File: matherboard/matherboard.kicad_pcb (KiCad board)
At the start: 2 copper layers, 17 parts, among them J1 RJ12, J2 RJ12, J3 RJ12, P1 VCC/GND, P2 CONN_01X02, P3 CONN_01X02, P4 CONN_01X02, P5 CONN_01X05, P6 CONN_01X02, U3 STAB3.3, U4 ESP8266

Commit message: Components for BUG
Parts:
- removed P1: VCC/GND, Pin_Headers:Pin_Header_Straight_1x02
- added CON1: BARREL_JACK, Connect:BARREL_JACK, F.Cu at (134.6, 121.9)
- added U1: button, bugs:button, F.Cu at (132.1, 81.9)
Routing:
- net Net-(CON1-Pad2): track 185.8 -> 269.5 mm
- net Net-(CON1-Pad1): track 0.00 -> 51.5 mm
- net (no net): track 39.9 -> 65.8 mm
- net Net-(J1-Pad1): track 173.4 -> 168.9 mm
- net Net-(J1-Pad5): track 120.5 -> 122.7 mm
- net Net-(P2-Pad2): track 5.08 -> 4.45 mm

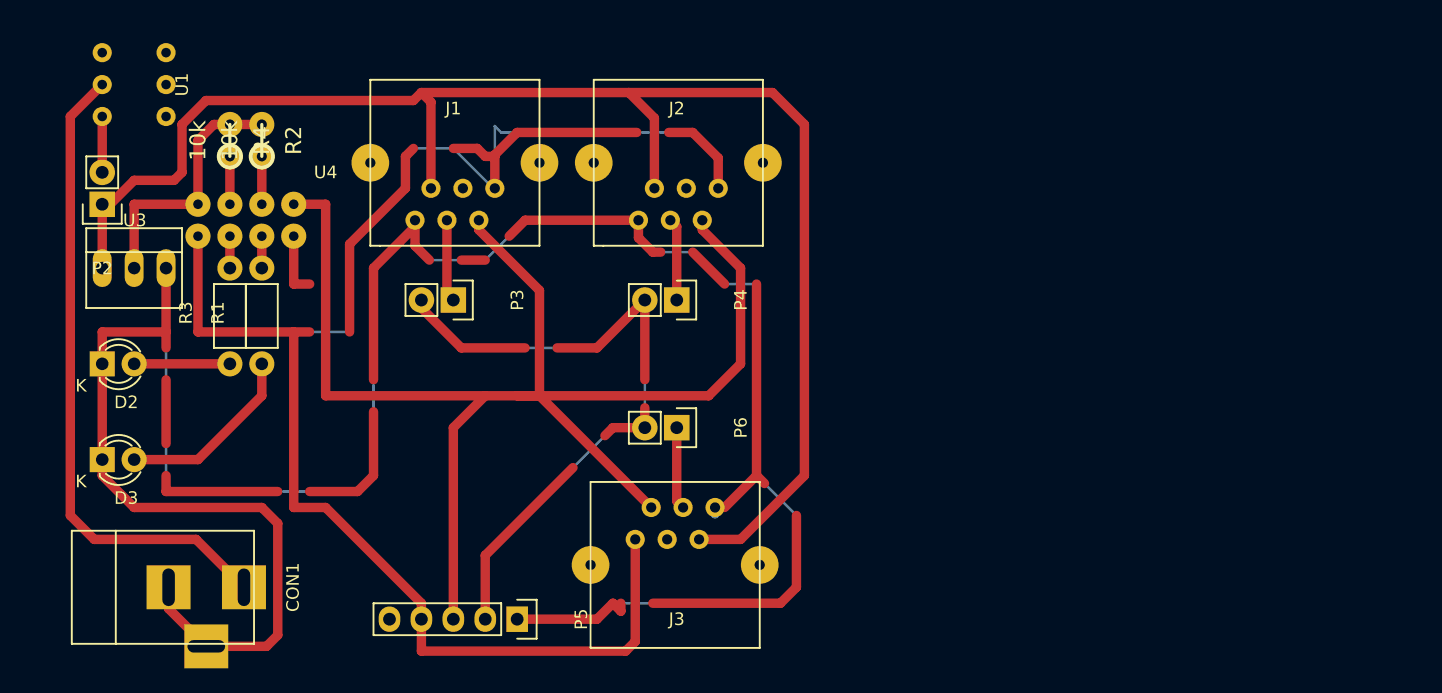
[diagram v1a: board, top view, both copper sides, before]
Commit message: Added power led to marherboard
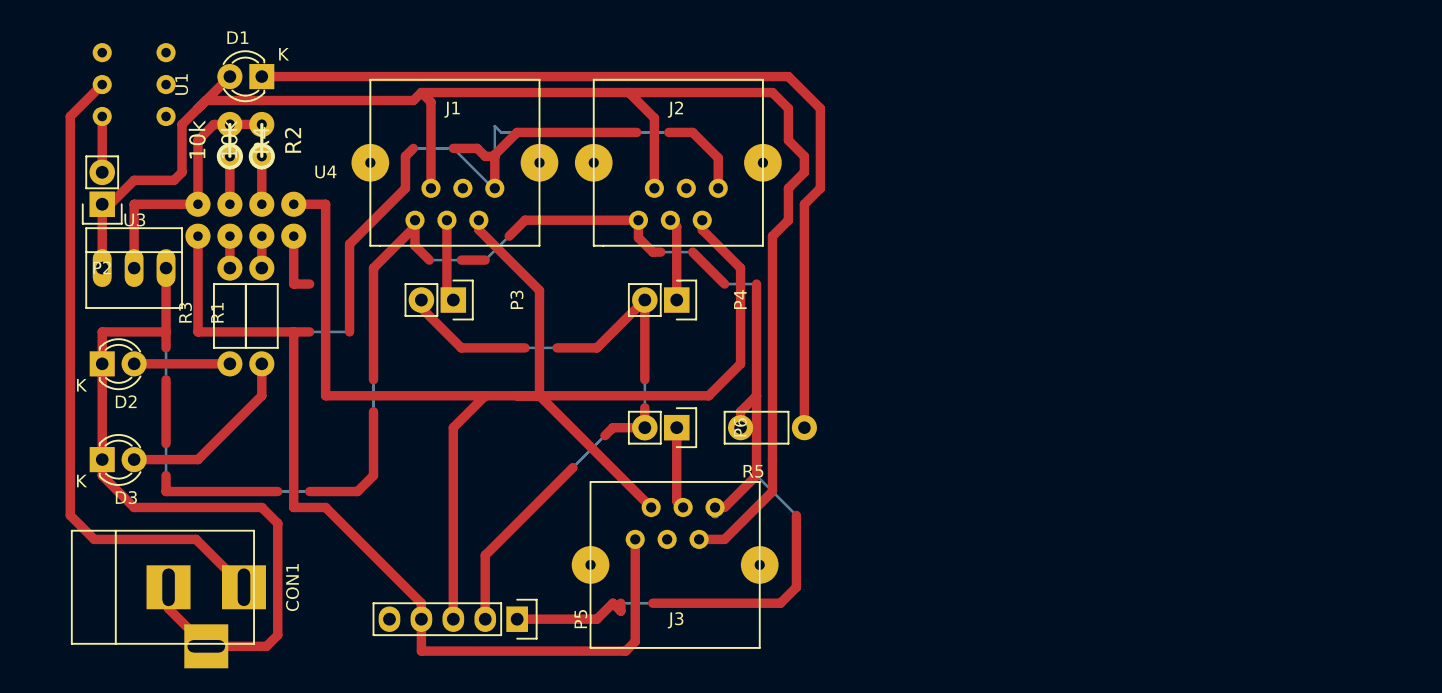
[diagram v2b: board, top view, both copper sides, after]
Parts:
- added D1: LED, LEDs:LED-3MM, F.Cu at (142.2, 81.3)
- added R5: 500, Resistors_ThroughHole:Resistor_Horizontal_RM7mm, F.Cu at (185.4, 109.2)
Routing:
- net Net-(D1-Pad1): track 0.00 -> 71.4 mm
- net Net-(D1-Pad2): track 122.7 -> 125.6 mm
- net Net-(CON1-Pad2): track 269.5 -> 271.6 mm

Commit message: Update WheelsAndIRT
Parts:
- R5: footprint Resistors_ThroughHole:Resistor_Horizontal_RM7mm -> Resistors_ThroughHole:Resistor_Horizontal_RM15mm
- moved J1 70.5 mm to (226.1, 100.3), turned to 0 degrees
- moved P3 61.0 mm to (218.4, 97.8), turned to 0 degrees
- moved R5 47.2 mm to (147.3, 81.3), turned to 270 degrees
- moved P5 46.4 mm to (208.3, 116.8), turned to 0 degrees
- moved J3 45.3 mm to (184.2, 80.0), turned to 180 degrees
- moved P6 17.0 mm to (182.9, 94.0), turned to 90 degrees
- moved P4 11.4 mm to (165.1, 94.0), turned to 90 degrees
- moved J2 10.9 mm to (165.1, 80.0)
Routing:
- net Net-(CON1-Pad2): track 271.6 -> 63.6 mm
- net Net-(J1-Pad1): track 168.9 -> 52.1 mm
- net Net-(J1-Pad2): track 113.7 -> 0.00 mm
- net Net-(P3-Pad2): track 99.2 -> 0.00 mm
- net Net-(D1-Pad2): track 125.6 -> 52.1 mm
- net Net-(D1-Pad1): track 71.4 -> 5.08 mm
- net (no net): track 65.8 -> 0.00 mm
- net Net-(J1-Pad4): track 6.56 -> 0.00 mm
- net Net-(J2-Pad4): track 6.56 -> 5.29 mm
- net Net-(J3-Pad4): track 6.56 -> 5.40 mm
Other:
- net class Default: trace_width 0.75 -> 0.4

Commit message: Schematics updates
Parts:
- P5: value CONN_01X05 -> CONN_01X04; footprint Pin_Headers:Pin_Header_Straight_1x05 -> Pin_Headers:Pin_Header_Straight_1x04
- moved P5 57.1 mm to (153.7, 100.3)
- moved J1 48.3 mm to (182.9, 121.9)
- moved P3 36.7 mm to (182.9, 106.7), turned to 270 degrees
- moved J2 2.54 mm to (165.1, 82.5)
- moved J3 2.54 mm to (184.2, 82.5)
- moved P4 2.54 mm to (165.1, 96.5)
- moved P6 2.54 mm to (182.9, 96.5)
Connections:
- P5 pad 1: Net-(CON1-Pad2) -> Net-(J1-Pad2)
- P5 pad 2: Net-(P3-Pad2) -> Net-(CON1-Pad2)
- P5 pad 3: Net-(J1-Pad2) -> Net-(J1-Pad1)
- P5 pad 4: Net-(J1-Pad1) -> Net-(P3-Pad2)
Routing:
- net Net-(J1-Pad1): track 52.1 -> 116.1 mm
- net Net-(J1-Pad2): track 0.00 -> 56.8 mm
- net Net-(CON1-Pad2): track 63.6 -> 114.0 mm
- net Net-(D1-Pad2): track 52.1 -> 98.0 mm
- net Net-(P3-Pad2): track 0.00 -> 20.4 mm
- net Net-(J1-Pad4): track 0.00 -> 6.56 mm
